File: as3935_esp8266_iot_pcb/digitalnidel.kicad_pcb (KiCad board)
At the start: 2 copper layers, 50 x 100 mm, 44 parts, among them K1 RELAY_2RT, K2 RELAY_2RT, P1 CONN_01X02, P10 CONN_01X03, P2 CONN_01X02, P3 CONN_01X02, P5 CONN_01X07, P6 CONN_01X03, P7 CONN_01X05, P8 CONN_01X06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

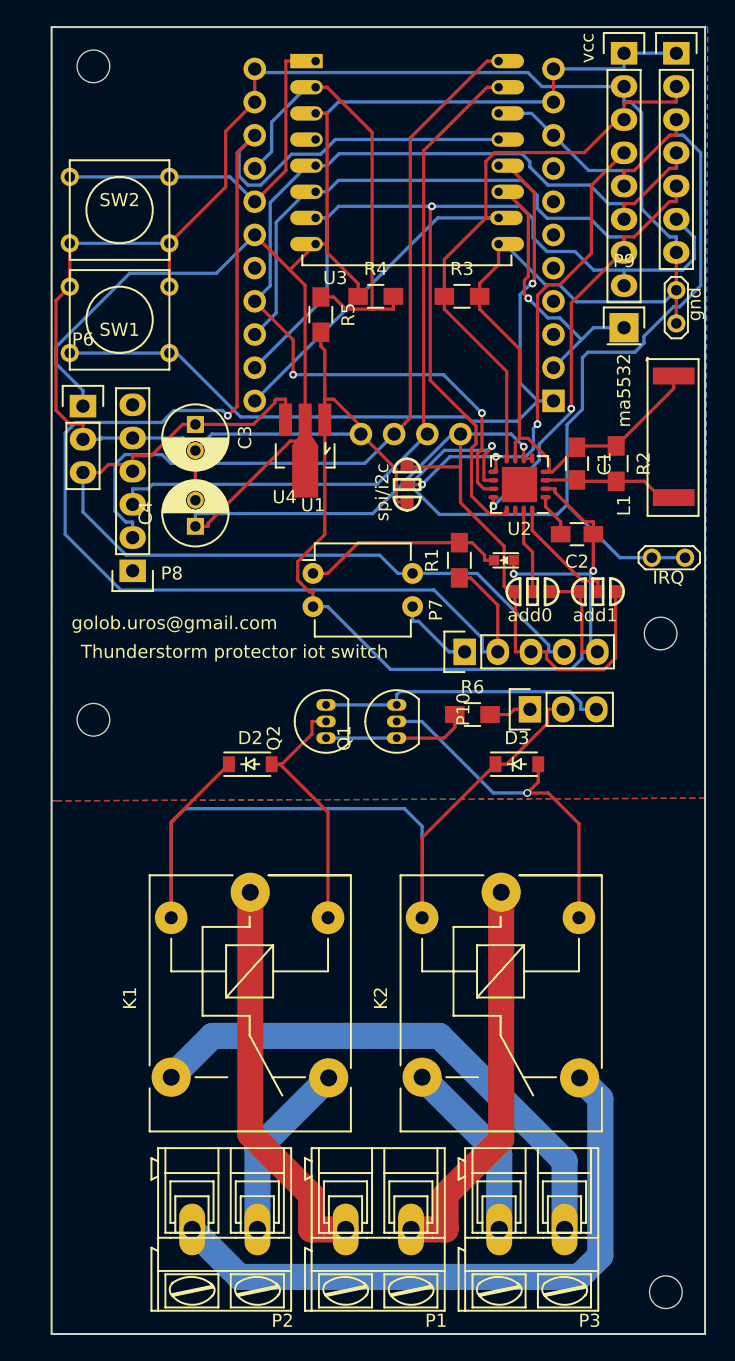
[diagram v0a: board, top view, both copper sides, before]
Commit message: added simple pcb containing only digital part with sensor and microcontroler module  with embedded wifi you'll have to add your own relays
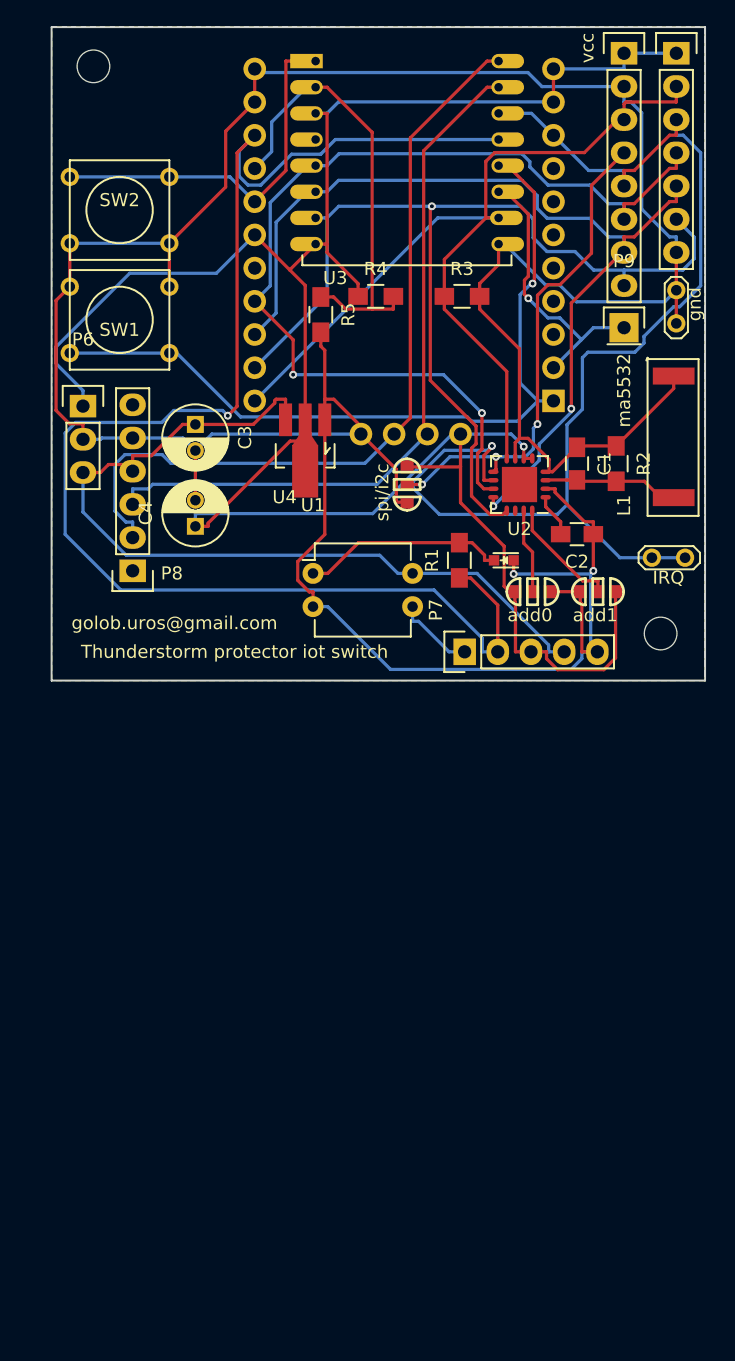
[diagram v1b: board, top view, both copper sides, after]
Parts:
- removed D2, D3: D, Diodes_SMD:SOD-123
- removed K1, K2: RELAY_2RT, ESP8266:relay
- removed P1, P2, P3: CONN_01X02, Connect:AK300-2
- removed P10: CONN_01X03, Pin_Headers:Pin_Header_Straight_1x03
- removed Q1, Q2: Q_NPN_BCE, Housings_TO-92:TO-92_Inline_Narrow_Oval
- removed R6: R, Resistors_SMD:R_0805_HandSoldering
- removed REF3, REF4: MountingHole_2-5mm, Mounting_Holes:MountingHole_2-5mm
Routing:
- net +5V: track 134.7 -> 65.0 mm
- net Net-(K2-Pad1): track 47.7 -> 0.00 mm
- net Net-(K1-Pad3): track 40.6 -> 0.00 mm
- net Net-(K1-Pad5): track 30.4 -> 0.00 mm
- net Net-(K2-Pad5): track 30.2 -> 0.00 mm
- net Net-(D3-Pad2): track 26.9 -> 0.00 mm, vias 1 -> 0
- net GND: track 281.6 -> 259.2 mm
- net Net-(D2-Pad2): track 19.4 -> 0.00 mm
- net Net-(K2-Pad3): track 14.1 -> 0.00 mm
- net Net-(K1-Pad1): track 13.9 -> 0.00 mm
- net Net-(Q1-Pad1): track 11.2 -> 0.00 mm
- net /to_switch: track 9.29 -> 6.07 mm
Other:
- board size 50 x 100 mm -> 50 x 50 mm
